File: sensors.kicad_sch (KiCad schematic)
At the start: 21 parts

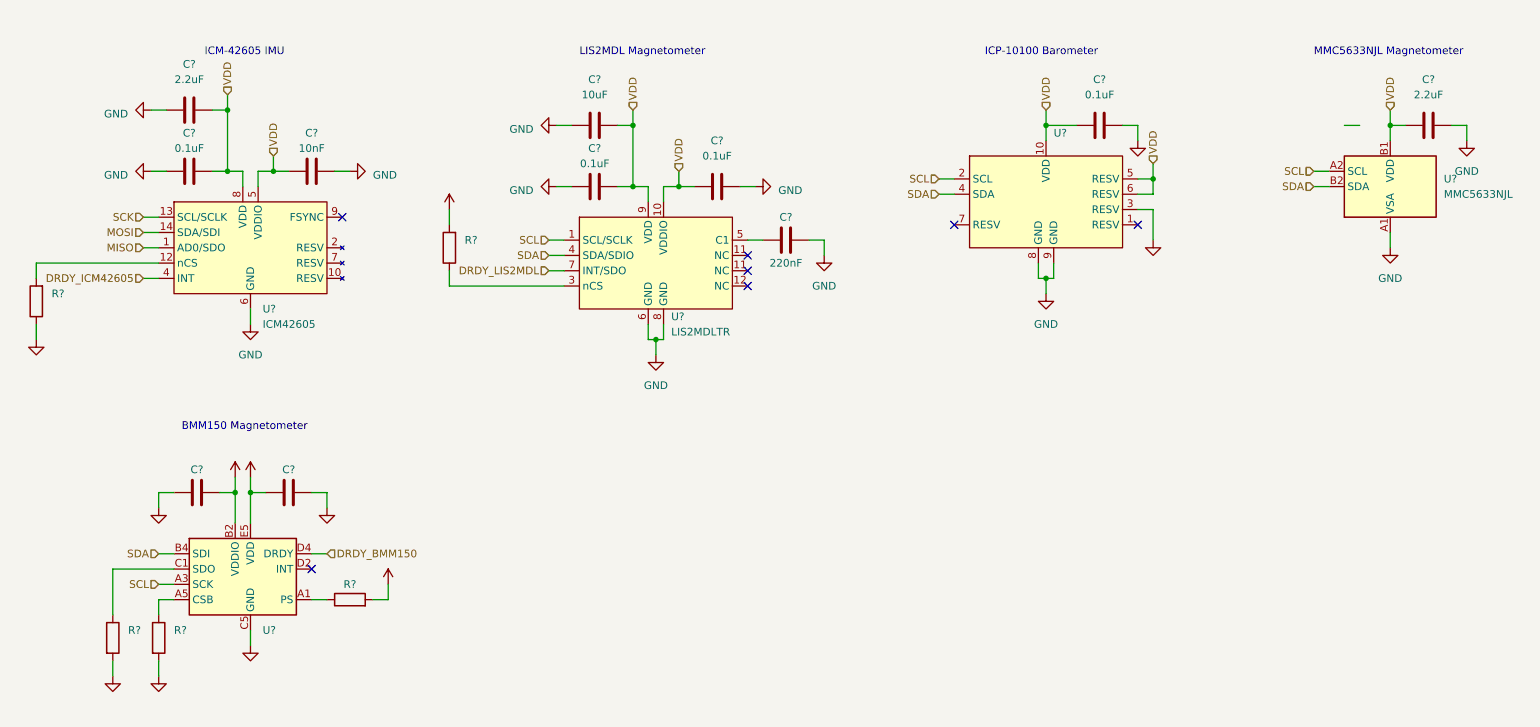
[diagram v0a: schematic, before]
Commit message: finish schematic draft
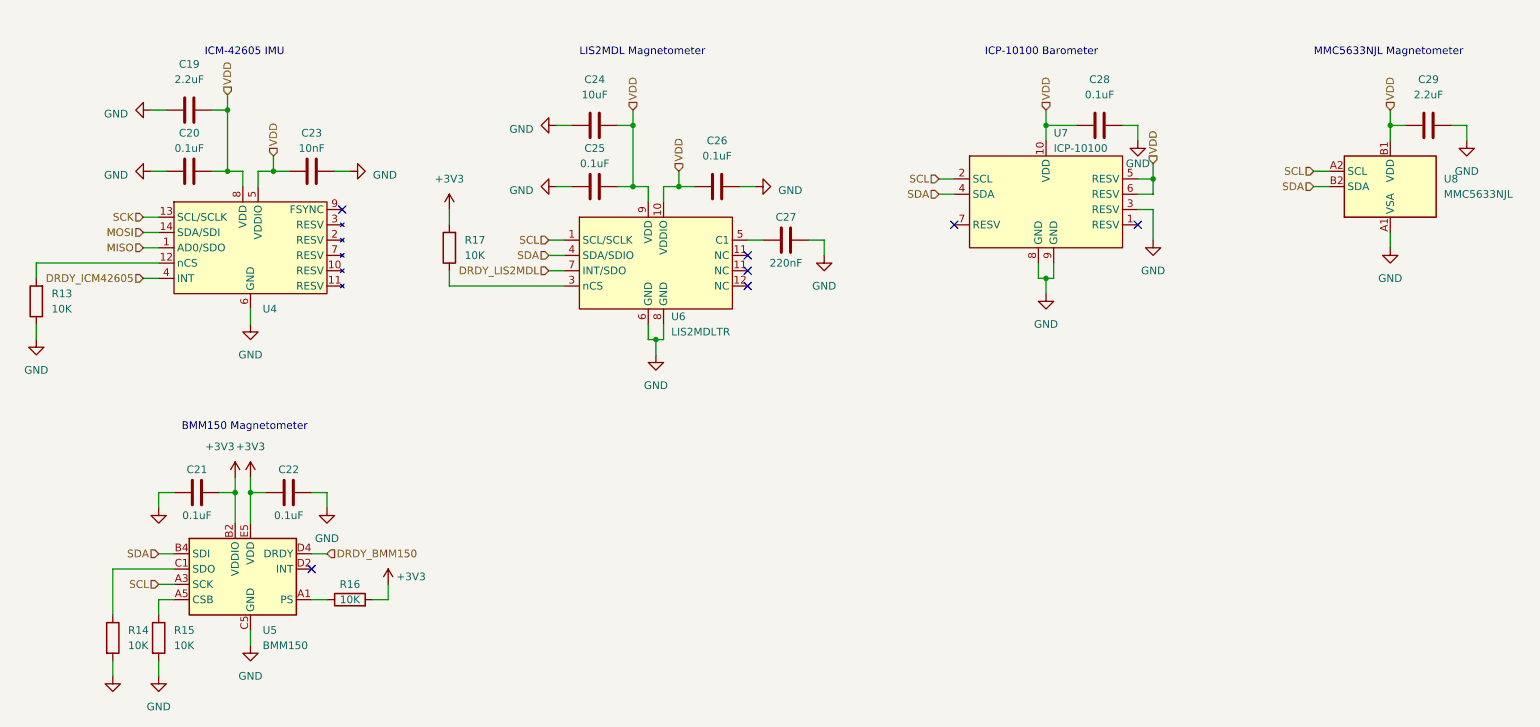
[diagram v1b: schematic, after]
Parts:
- C21, C22: renamed from C?; value (none) -> 0.1uF
- R13, R14, R15, R16, R17: renamed from R?; value (none) -> 10K
- U4: renamed from U?; value ICM42605 -> (none)
- U5: renamed from U?; value (none) -> BMM150; footprint (none) -> Package_CSP:WLCSP-12_1.56x1.56mm_P0.4mm
- U7: renamed from U?; value (none) -> ICP-10100; footprint ICP20100:PQFN50P200X200X85-10N -> (none)
- gave numbers to parts that had none: 11
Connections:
- net at U4.10 (RESV): no longer U4.11 (RESV)
- net at U4.2 (RESV): no longer U4.3 (RESV)

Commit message: schematic: update regulator, sensors
* simplify some sensor schematics
* replace 3v3 regulator
* DRC and footprints
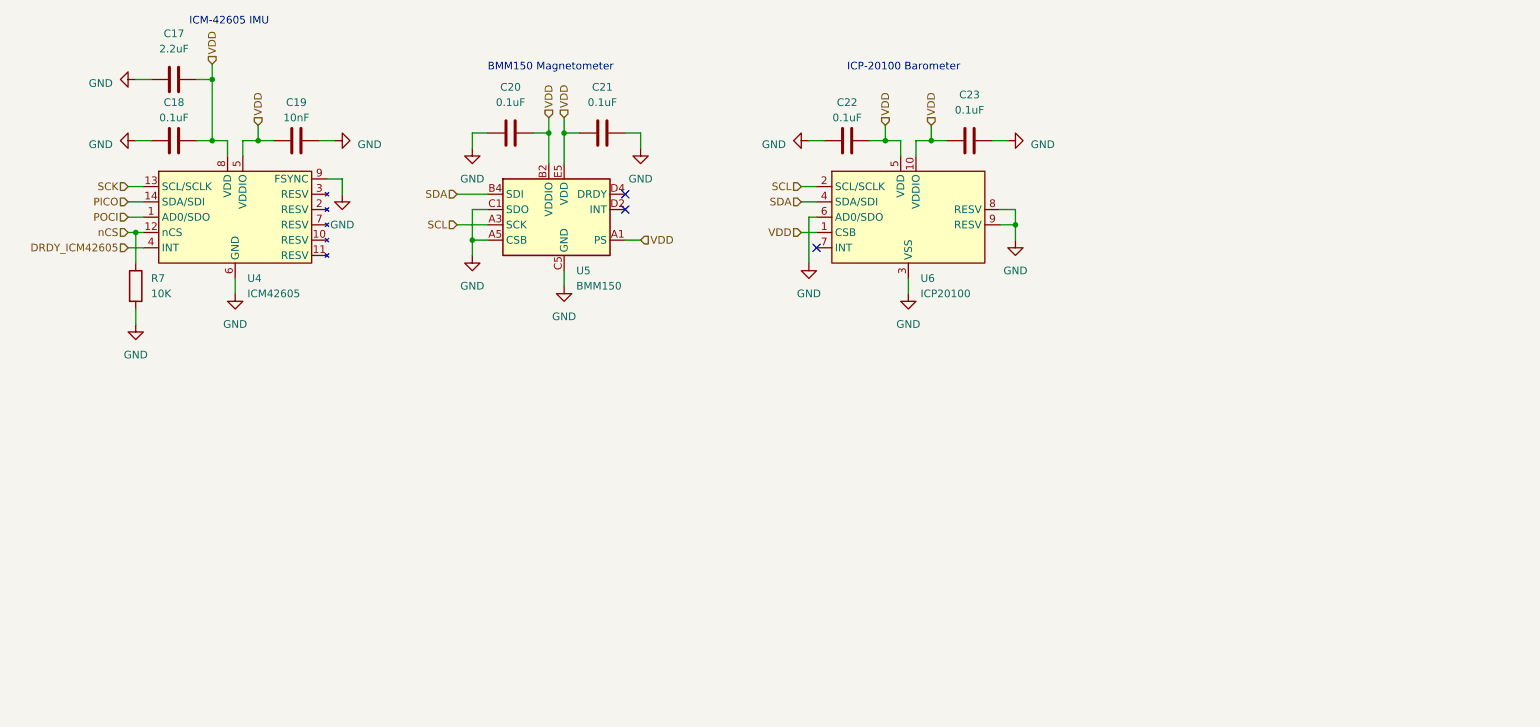
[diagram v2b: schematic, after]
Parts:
- removed C24: 10uF, Capacitor_SMD:C_0402_1005Metric, symbol Device:C
- removed C25, C26, C28: 0.1uF, Capacitor_SMD:C_0402_1005Metric, symbol Device:C
- removed C27: 220nF, Capacitor_SMD:C_0402_1005Metric, symbol Device:C
- removed C29: 2.2uF, Capacitor_SMD:C_0402_1005Metric, symbol Device:C
- removed R13, R14, R15, R16, R17: 10K, symbol Device:R
- removed U6: LIS2MDLTR, Package_LGA:LGA-12_2x2mm_P0.5mm, symbol LIS2MDL:LIS2MDLTR
- removed U7: ICP-10100, symbol Sensors:ICP-10100
- removed U8: MMC5633NJL, Package_BGA:WLP-4_0.86x0.86mm_P0.4mm, symbol Sensor_Magnetic:MMC5633NJL
- added C17: 2.2uF, Capacitor_SMD:C_0402_1005Metric, symbol Device:C
- added C18: 0.1uF, Capacitor_SMD:C_0402_1005Metric, symbol Device:C
- added R7: 10K, Resistor_SMD:R_0402_1005Metric, symbol Device:R
- added U6: ICP20100, ICP20100:PQFN50P200X200X85-10N, symbol Invensense_ICP:ICP20100
- C19: value 2.2uF -> 10nF; LCSC C23733 -> C15195
- C20: LCSC C1525 -> (none)
- C21: footprint (none) -> Capacitor_SMD:C_0402_1005Metric
- C22: footprint (none) -> Capacitor_SMD:C_0402_1005Metric; LCSC (none) -> C1525
- C23: value 10nF -> 0.1uF
- U4: value (none) -> ICM42605
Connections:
- net GND: now also C19.2, C22.1, U4.9 (FSYNC), U5.A5 (CSB), U5.C1 (SDO), C17.1, C18.1, R7.2, U6.3 (VSS), U6.6 (AD0/SDO), U6.8 (RESV), U6.9 (RESV); no longer C19.1, C22.2
- net SCL: now also U6.2 (SCL/SCLK)
- net SDA: now also U6.4 (SDA/SDI)
- net VDD: now also C19.1, C21.1, C22.2, U5.A1 (PS), U5.B2 (VDDIO), U5.E5 (VDD), C17.2, C18.2, U6.1 (CSB), U6.10 (VDDIO), U6.5 (VDD); no longer C19.2
- net nCS: now reaches U4.12 (nCS)
- net nCS: now also R7.1
- removed net +3V3: C21.1, C22.1, U5.B2 (VDDIO), U5.E5 (VDD)
- net DRDY_BMM150: no longer names the net of U5.D4 (DRDY)
- net MISO renamed POCI
- net MOSI renamed PICO
- no-connect marks 7 -> 3
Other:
- note added: "ICP-20100 Barometer"
- note removed: "ICP-10100 Barometer"
- note removed: "LIS2MDL Magnetometer"
- note removed: "MMC5633NJL Magnetometer"

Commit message: a little more work
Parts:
- removed C21: 0.1uF, Capacitor_SMD:C_0402_1005Metric, symbol Device:C
- removed U5: BMM150, Package_CSP:WLCSP-12_1.56x1.56mm_P0.4mm, symbol Sensor_Magnetic:BMM150
- added C12: 1uF, Capacitor_SMD:C_0402_1005Metric, symbol Device:C
- added R8, R9: 2.7K, Resistor_SMD:R_0402_1005Metric, symbol Device:R
- added U5: MMC5983MA, Package_LGA:LGA-16_3x3mm_P0.5mm, symbol MMC5983MA:MMC5983MA
- C20: value 0.1uF -> 10uF
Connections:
- net GND: now also C20.2, C12.1, U5.11 (GND), U5.9 (GND); no longer C20.1
- net SCL: now also R8.2, U5.1 (SCL)
- net SDA: now also R9.2, U5.16 (SDA)
- net VDD: now also C12.2, R8.1, R9.1, U5.13 (VDDIO), U5.2 (VDD), U5.4 (~{CS}); no longer C20.2
- new net: C20.1, U5.10 (CAP)
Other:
- note added: "MMC5983MA Magnetometer"
- note removed: "BMM150 Magnetometer"
